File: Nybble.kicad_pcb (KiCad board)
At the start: 2 copper layers, 250.4 x 79 mm, 106 parts, among them J1 USB_mini_micro_B, SW1 SW_PUSH, U1 ATMEGA32U4, X1 XTAL_GND

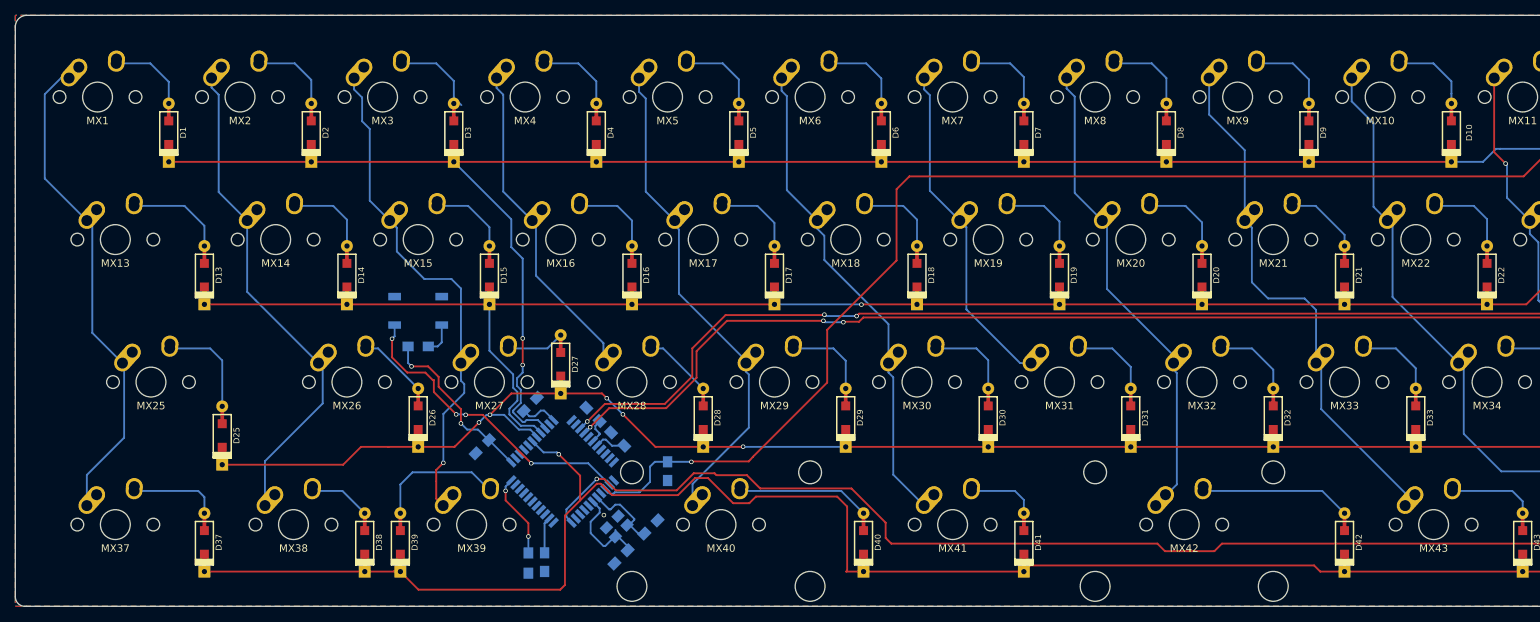
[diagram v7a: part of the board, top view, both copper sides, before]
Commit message: Routed all columnar traces
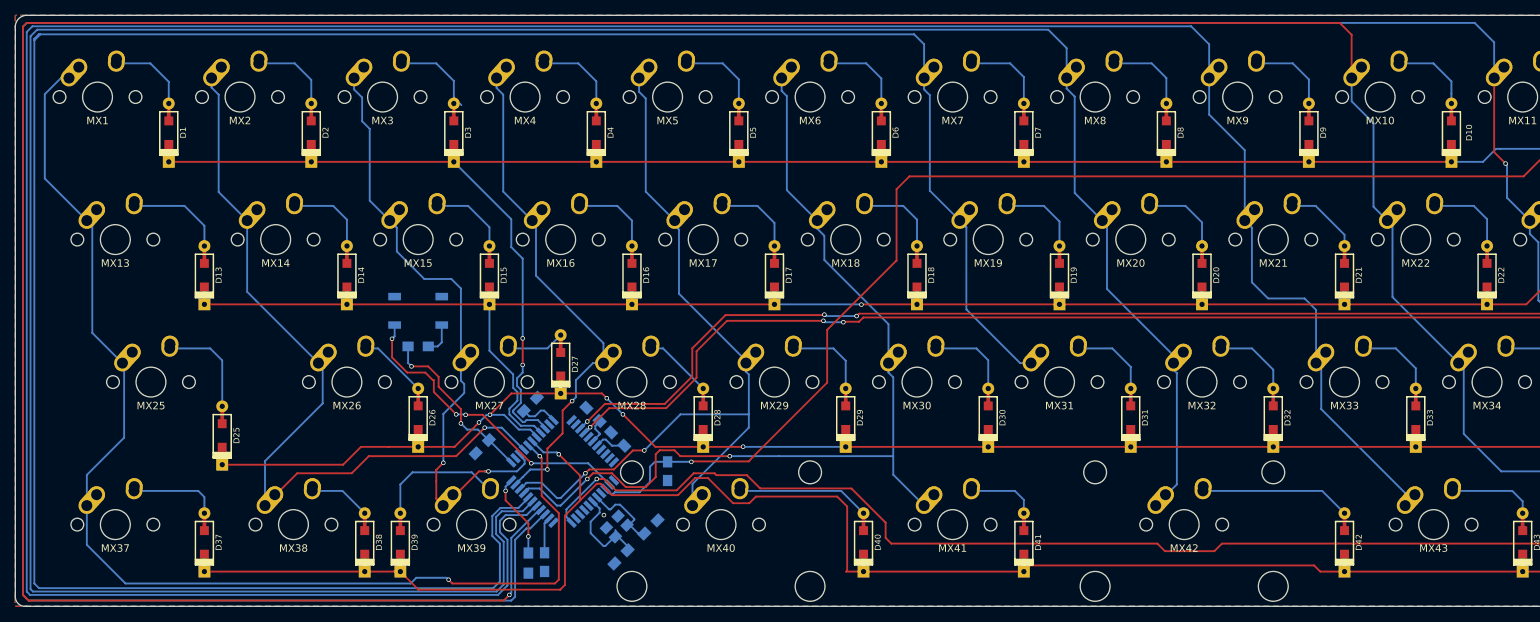
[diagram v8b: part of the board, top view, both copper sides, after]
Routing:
- net /Col10: track 44.0 -> 402.0 mm
- net /Col9: track 73.7 -> 412.8 mm, vias 0 -> 1
- net /Col8: track 72.1 -> 390.5 mm
- net /Col7: track 64.4 -> 361.1 mm
- net /Col6: track 44.9 -> 322.0 mm
- net /Col0: track 65.6 -> 156.6 mm, vias 0 -> 2
- net /Col5: track 65.0 -> 122.3 mm, vias 0 -> 2
- net /Col1: track 66.5 -> 106.7 mm, vias 0 -> 1
- net /Col4: track 66.3 -> 102.8 mm, vias 0 -> 2
- net /Col3: track 44.0 -> 67.3 mm, vias 0 -> 2
- net /Col2: track 67.3 -> 83.1 mm, vias 1 -> 2
